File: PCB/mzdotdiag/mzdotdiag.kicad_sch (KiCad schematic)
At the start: 1 part, among them J1 Conn_01x25

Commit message: advancements in schematic
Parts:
- added Q1: Q_NPN_BEC, symbol Device:Q_NPN_BEC
- added U1: 4050, symbol 4xxx:4050
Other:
- note added: "B+ - 12V"
- note added: "F/P - Activate Fuel Pump Relay - Pull down to GND"
- note added: "FAB - Airbag SRS System - Feedback from SRS"
- note added: "FAT - Automatic Transmission - Feedback pin for AT"
- note added: "FBS - ABS System - Feedback from ABS"
- note added: "FEN - 0...12V - Low Active CEL Light"
- note added: "FSC - Cruise Control System - Cruise Control System Feedback Pin"
- note added: "IG- - Rev Counter (RPM = 30/delta[T])"
- note added: "MEN - ???"
- note added: "TAB - Airbag SRS System - Pull down to GND for starting test"
- note added: "TAT - Automatic Transmission - Pull down to GND to start test"
- note added: "TBS - ABS System - Pull down to GND for starting test"
- note added: "TEN - Test engine - Pull down the GND for starting test"
- note added: "TFA - Test Fan - Pull down to GND to start Fan"
- note added: "TSC - Cruise Control System - Test Cruise Control System"
- moved on the sheet: J1

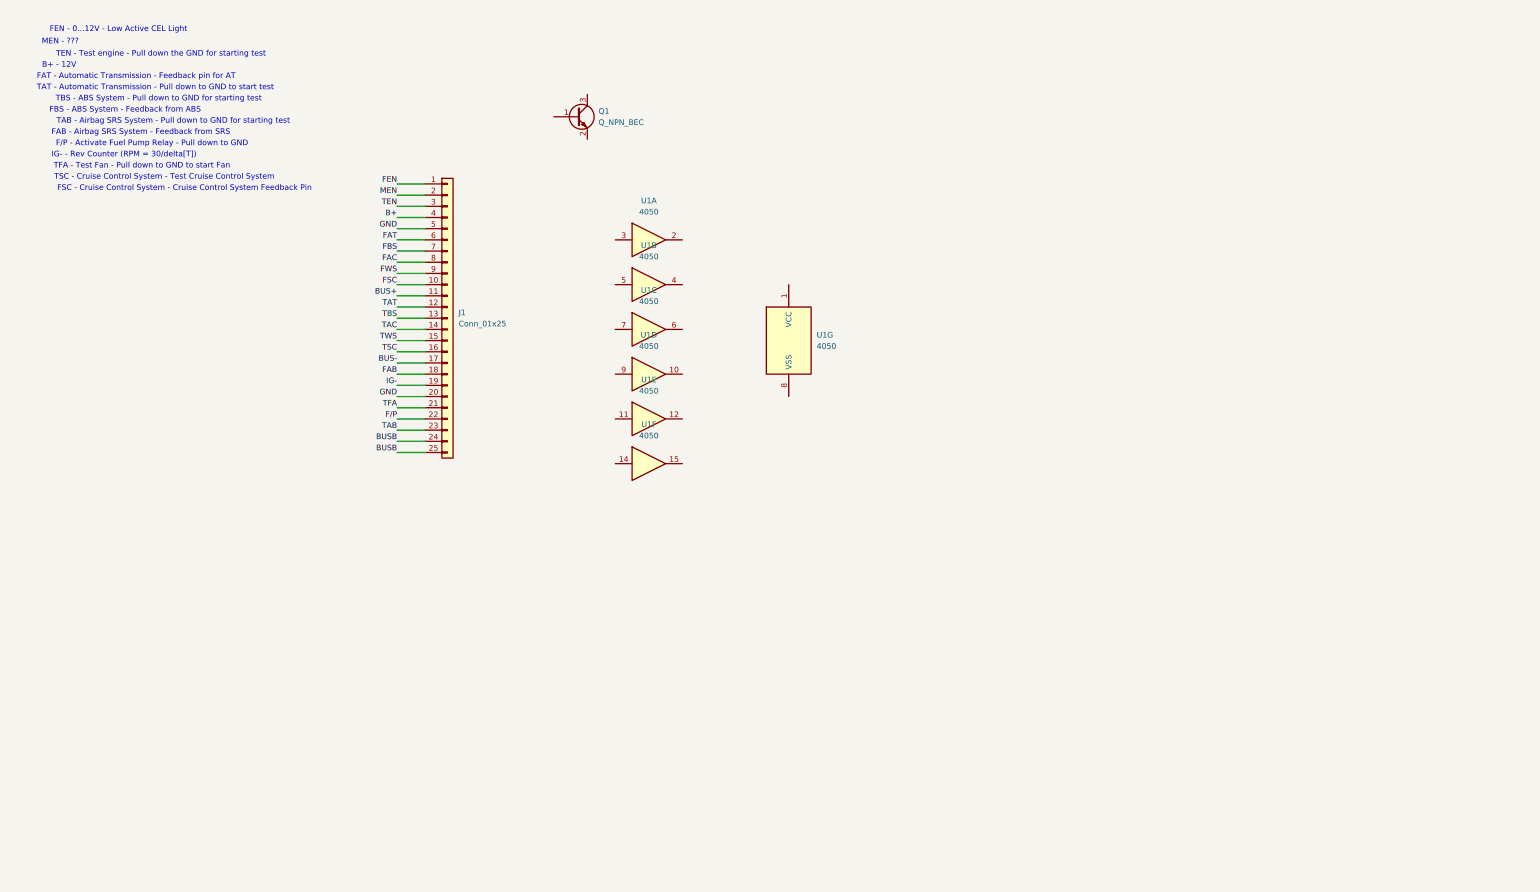
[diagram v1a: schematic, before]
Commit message: Schematic updates
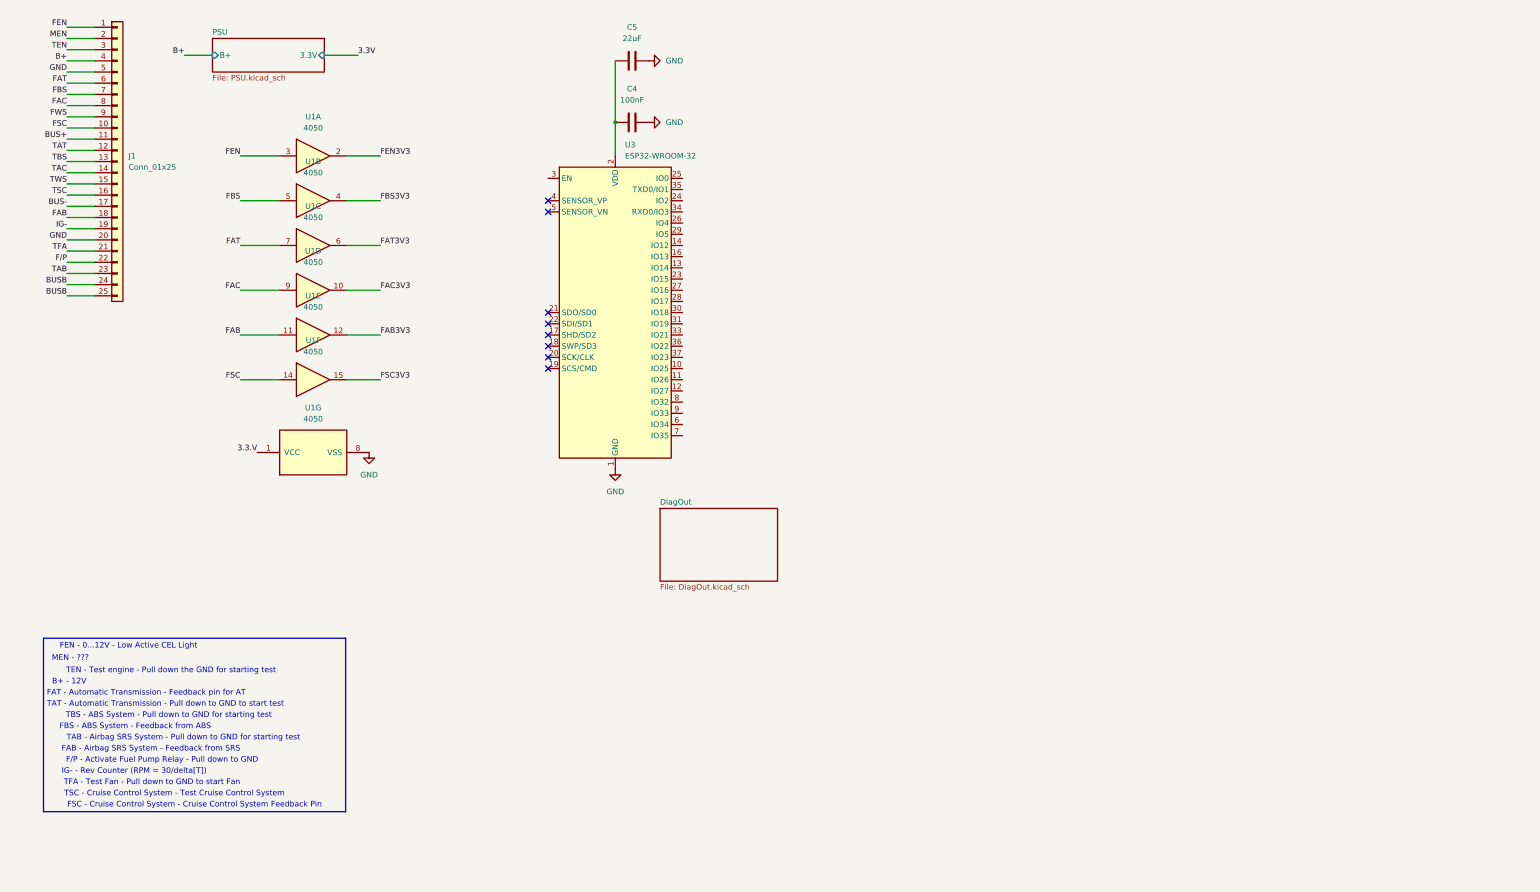
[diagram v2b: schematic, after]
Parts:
- removed Q1: Q_NPN_BEC, symbol Device:Q_NPN_BEC
- added C4: 100nF, symbol Device:C
- added C5: 22uF, symbol Device:C
- added U3: ESP32-WROOM-32, RF_Module:ESP32-WROOM-32, symbol RF_Module:ESP32-WROOM-32
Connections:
- net FAB: now also U1.11
- net FAC: now also U1.9
- net FAT: now also U1.7
- net FBS: now also U1.5
- net FEN: now also U1.3
- net FSC: now also U1.14
- net GND: now also U1.8 (VSS), C4.2, C5.2, U3.1 (GND), U3.15 (GND), U3.38 (GND), U3.39 (GND)
- net FBS3V3: now reaches U1.4
- net FSC3V3: now reaches U1.15
- net FAB3V3: now reaches U1.12
- net 3.3.V: now reaches U1.1 (VCC)
- net FAC3V3: now reaches U1.10
- net FAT3V3: now reaches U1.6
- net FEN3V3: now reaches U1.2
- new net: C4.1, C5.1, U3.2 (VDD)
- no-connect marks 0 -> 8
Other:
- added sheet DiagOut (DiagOut.kicad_sch)
- added sheet PSU (PSU.kicad_sch)
- moved on the sheet: J1, U1A, U1B, U1C, U1D, U1E, U1F, U1G

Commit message: Lots of schematic updates, found CD4504B for logic level shifting
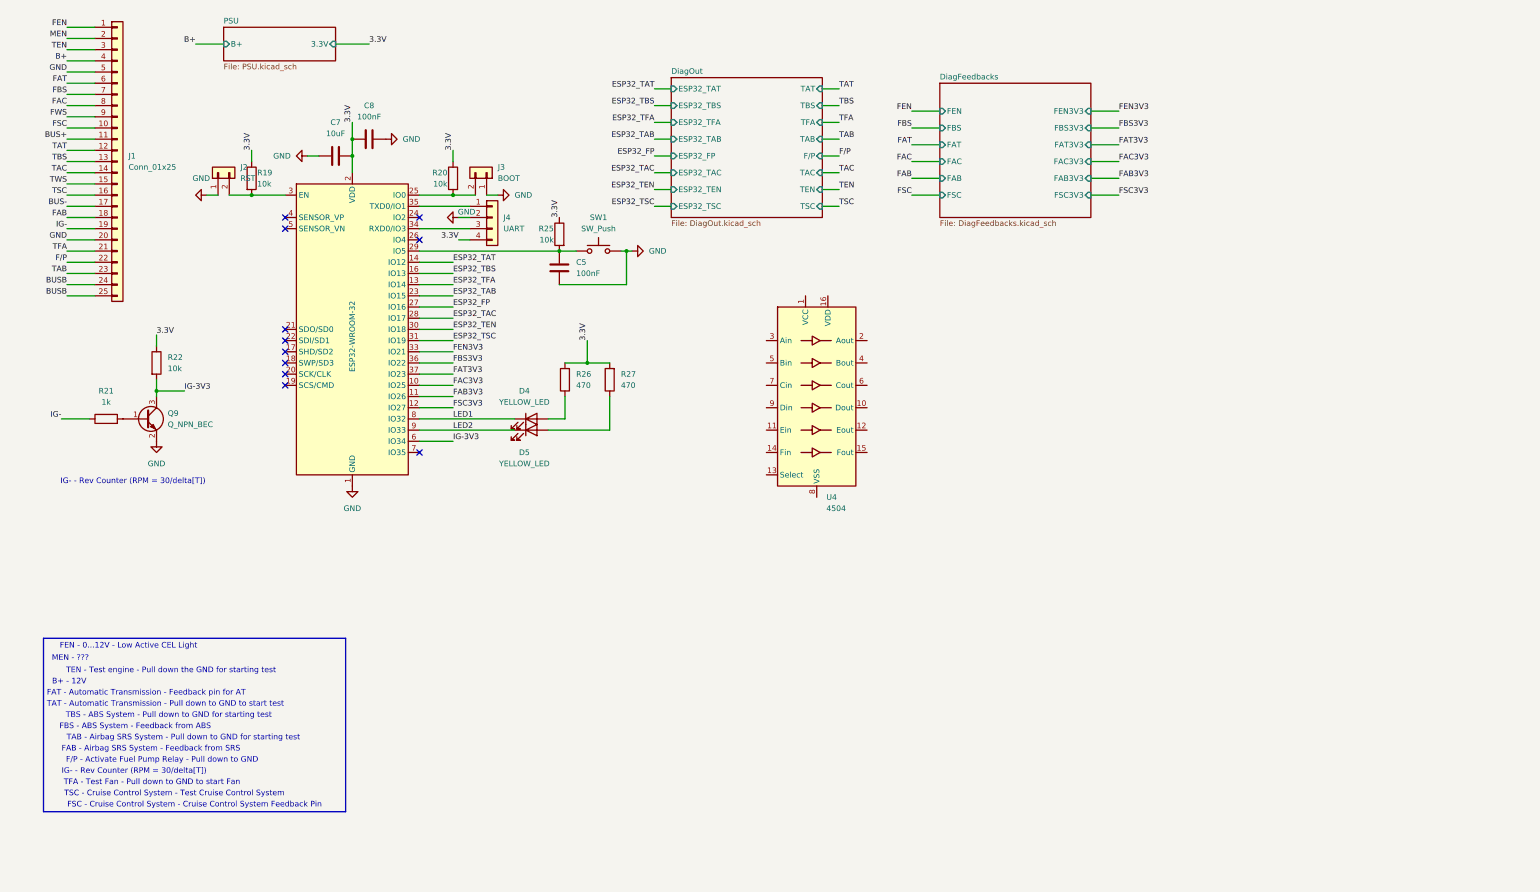
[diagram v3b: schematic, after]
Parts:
- removed C4: 100nF, symbol Device:C
- removed U1: 4050, symbol 4xxx:4050
- added C7: 10uF, Capacitor_SMD:C_0805_2012Metric, symbol Device:C
- added C8: 100nF, Capacitor_SMD:C_0603_1608Metric, symbol Device:C
- added D4, D5: YELLOW_LED, LED_SMD:LED_0805_2012Metric, symbol Device:LED
- added J2: RST, Button_Switch_SMD:SW_SPST_CK_RS282G05A3, symbol Connector_Generic:Conn_01x02
- added J3: BOOT, Button_Switch_SMD:SW_SPST_CK_RS282G05A3, symbol Connector_Generic:Conn_01x02
- added J4: UART, Connector_PinHeader_2.54mm:PinHeader_1x04_P2.54mm_Vertical, symbol Connector_Generic:Conn_01x04
- added Q9: Q_NPN_BEC, Package_TO_SOT_SMD:SOT-23, symbol Device:Q_NPN_BEC
- added R19, R20, R22, R25: 10k, Resistor_SMD:R_0603_1608Metric, symbol Device:R
- added R21: 1k, Resistor_SMD:R_0603_1608Metric, symbol Device:R
- added R26, R27: 470, Resistor_SMD:R_0603_1608Metric_Pad0.98x0.95mm_HandSolder, symbol Device:R
- added SW1: SW_Push, Button_Switch_SMD:SW_SPST_CK_RS282G05A3, symbol Switch:SW_Push
- added U4: 4504, symbol 4xxx:4504
- C5: value 22uF -> 100nF; footprint (none) -> Capacitor_SMD:C_0603_1608Metric; LOMEX (none) -> 82-13-28
- J1: footprint (none) -> mykicad_6:MazdaNADiag; Mouser (none) -> 651-1945193
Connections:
- net 3.3V: now also U3.2 (VDD), C7.1, C8.1, J4.4 (Pin_4), R19.1, R20.1, R22.1, R25.1, R26.2, R27.2
- net FAB3V3: now also U3.11 (IO26)
- net FAC3V3: now also U3.10 (IO25)
- net FAT3V3: now also U3.37 (IO23)
- net FBS3V3: now also U3.36 (IO22)
- net FEN3V3: now also U3.33 (IO21)
- net FSC3V3: now also U3.12 (IO27)
- net GND: now also C5.1, C7.2, C8.2, J2.1 (Pin_1), J3.1 (Pin_1), J4.2 (Pin_2), Q9.2 (E), SW1.2; no longer C5.2
- net IG-: now also R21.1
- net ESP32_TFA: now reaches U3.13 (IO14)
- net ESP32_TAT: now reaches U3.14 (IO12)
- net ESP32_TBS: now reaches U3.16 (IO13)
- net ESP32_TAB: now reaches U3.23 (IO15)
- net at U3.25 (IO0): now also J3.2 (Pin_2), R20.2
- net ESP32_FP: now reaches U3.27 (IO16)
- net ESP32_TAC: now reaches U3.28 (IO17)
- net at U3.29 (IO5): now also C5.2, R25.2, SW1.1
- net at U3.3 (EN): now also J2.2 (Pin_2), R19.2
- net ESP32_TEN: now reaches U3.30 (IO18)
- net ESP32_TSC: now reaches U3.31 (IO19)
- net at U3.34 (RXD0/IO3): now also J4.3 (Pin_3)
- net at U3.35 (TXD0/IO1): now also J4.1 (Pin_1)
- net IG-3V3: now reaches U3.6 (IO34)
- net IG-3V3: now also Q9.3 (C), R22.2
- net LED1: now reaches U3.8 (IO32)
- net LED1: now also D4.1 (K)
- net LED2: now reaches U3.9 (IO33)
- net LED2: now also D5.1 (K)
- new net: Q9.1 (B), R21.2
- new net: D4.2 (A), R26.1
- new net: D5.2 (A), R27.1
- no-connect marks 8 -> 11
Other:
- added sheet DiagFeedbacks (DiagFeedbacks.kicad_sch)
- sheet DiagOut ports: added ESP32_FP, ESP32_TAB, ESP32_TAC, ESP32_TAT, ESP32_TBS, ESP32_TEN, ESP32_TFA, ESP32_TSC, F/P, TAB, TAC, TAT, TBS, TEN, TFA, TSC; removed none

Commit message: schematic and pcb update with new levelshifter IC
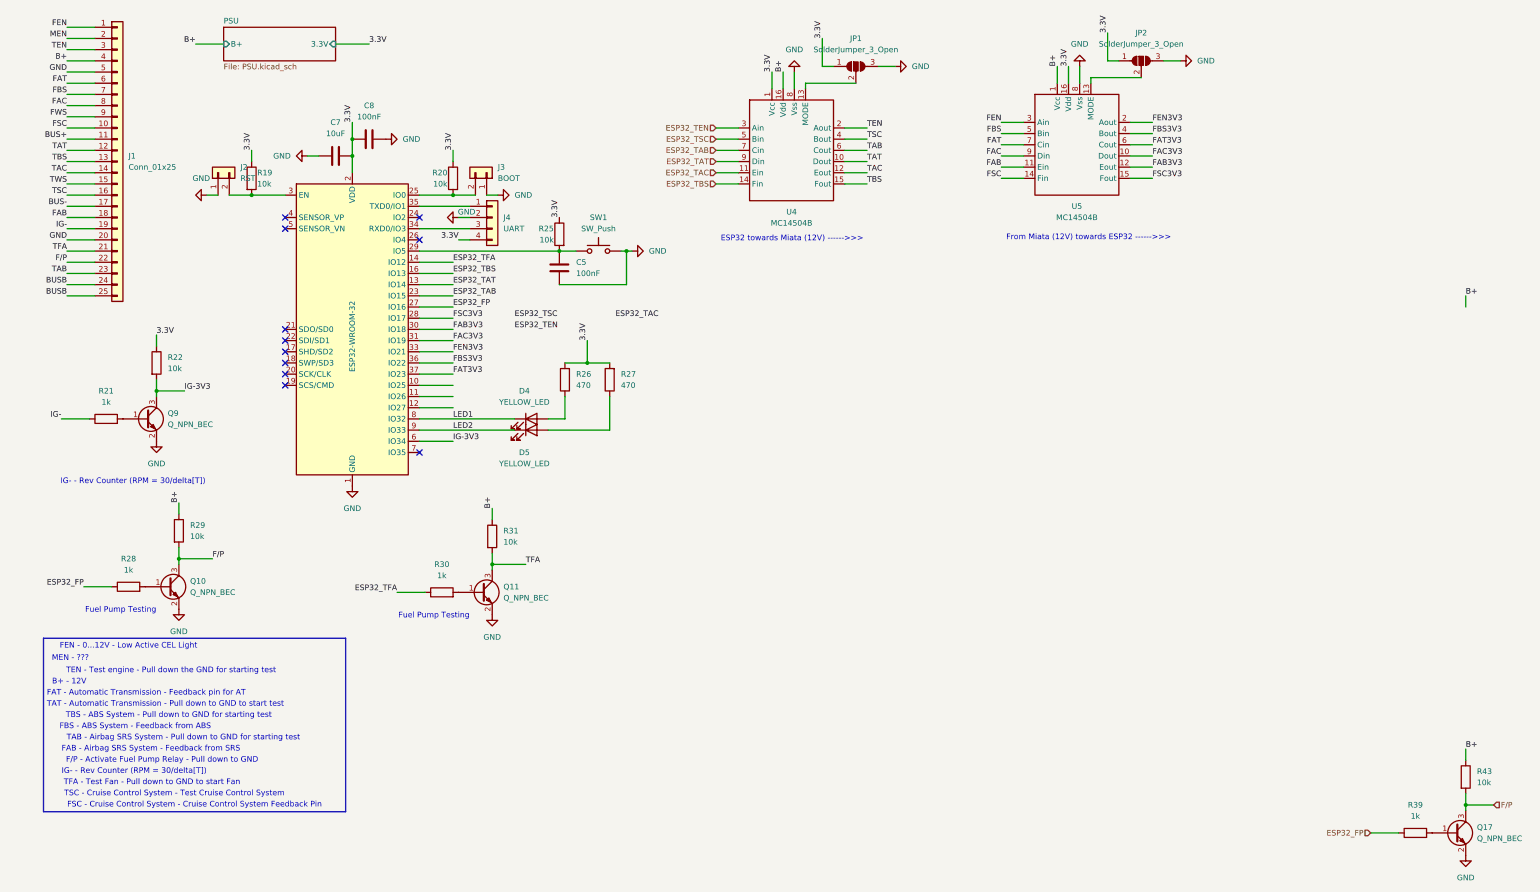
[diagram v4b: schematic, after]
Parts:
- removed U4: 4504, symbol 4xxx:4504
- added JP1, JP2: SolderJumper_3_Open, Jumper:SolderJumper-3_P1.3mm_Open_RoundedPad1.0x1.5mm, symbol Jumper:SolderJumper_3_Open
- added Q10, Q11, Q17: Q_NPN_BEC, Package_TO_SOT_SMD:SOT-23, symbol Device:Q_NPN_BEC
- added R28, R30, R39: 1k, Resistor_SMD:R_0603_1608Metric, symbol Device:R
- added R29, R31, R43: 10k, Resistor_SMD:R_0603_1608Metric, symbol Device:R
- added U4, U5: MC14504B, Package_SO:SOIC-16_3.9x9.9mm_P1.27mm, symbol local_lib:MC14504
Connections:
- net 3.3V: now also JP1.1 (A), JP2.1 (A), U4.1 (Vcc), U5.16 (Vdd)
- net B+: now also R29.1, R31.1, R43.1, U4.16 (Vdd), U5.1 (Vcc)
- net ESP32_FP: now also R28.1, R39.1
- net ESP32_TAB: now also U4.7 (Cin)
- net ESP32_TAC: now also U4.11 (Ein); no longer U3.28 (IO17)
- net ESP32_TAT: now also U3.13 (IO14), U4.9 (Din); no longer U3.14 (IO12)
- net ESP32_TBS: now also U4.14 (Fin)
- net ESP32_TEN: now also U4.3 (Ain); no longer U3.30 (IO18)
- net ESP32_TFA: now also U3.14 (IO12), R30.1; no longer U3.13 (IO14)
- net ESP32_TSC: now also U4.5 (Bin); no longer U3.31 (IO19)
- net FAB: now also U5.11 (Ein)
- net FAB3V3: now also U3.30 (IO18), U5.12 (Eout); no longer U3.11 (IO26)
- net FAC: now also U5.9 (Din)
- net FAC3V3: now also U3.31 (IO19), U5.10 (Dout); no longer U3.10 (IO25)
- net FAT: now also U5.7 (Cin)
- net FAT3V3: now also U5.6 (Cout)
- net FBS: now also U5.5 (Bin)
- net FBS3V3: now also U5.4 (Bout)
- net FEN: now also U5.3 (Ain)
- net FEN3V3: now also U5.2 (Aout)
- net FSC: now also U5.14 (Fin)
- net FSC3V3: now also U3.28 (IO17), U5.15 (Fout); no longer U3.12 (IO27)
- net F/P: now also Q10.3 (C), Q17.3 (C), R29.2, R43.2
- net GND: now also JP1.3 (B), JP2.3 (B), Q10.2 (E), Q11.2 (E), Q17.2 (E), U4.8 (Vss), U5.8 (Vss)
- net TAB: now also U4.6 (Cout)
- net TAC: now also U4.12 (Eout)
- net TAT: now also U4.10 (Dout)
- net TBS: now also U4.15 (Fout)
- net TEN: now also U4.2 (Aout)
- net TFA: now also Q11.3 (C), R31.2
- net TSC: now also U4.4 (Bout)
- new net: Q10.1 (B), R28.2
- new net: JP1.2 (C), U4.13 (MODE)
- new net: JP2.2 (C), U5.13 (MODE)
- new net: Q11.1 (B), R30.2
- new net: Q17.1 (B), R39.2
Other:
- removed sheet DiagFeedbacks
- removed sheet DiagOut
- note added: "ESP32 towards Miata (12V) ------>>>"
- note added: "From Miata (12V) towards ESP32 ------>>>"
- note added: "Fuel Pump Testing"

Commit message: pcb upd
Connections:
- net ESP32_TAB: now also U3.14 (IO12); no longer U3.23 (IO15)
- net ESP32_TBS: no longer U3.16 (IO13)
- net ESP32_TEN: now also U3.23 (IO15)
- net ESP32_TFA: no longer U3.14 (IO12)
- net ESP32_TSC: now also U3.16 (IO13)
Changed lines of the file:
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@@
-		)
-	)
-	(label "ESP32_TBS"
-		(at 107.95 72.39 0)
-		(effects
-			(font
-				(size 1.27 1.27)
-			)
-			(justify left bottom)
 		)
 	)
@@
 		)
 	)
+	(label "ESP32_TFA"
+		(at 138.43 81.28 0)
+		(effects
+			(font
+				(size 1.27 1.27)
+			)
+			(justify left bottom)
+		)
+	)
 	(label "FEN3V3"
 		(at 266.7 38.1 0)
@@
 		)
 	)
-	(label "ESP32_TAB"
-		(at 107.95 77.47 0)
-		(effects
-			(font
-				(size 1.27 1.27)
-			)
-			(justify left bottom)
-		)
-	)
 	(label "FAT"
 		(at 20.32 29.21 180)
@@
 		)
 	)
+	(label "ESP32_TAB"
+		(at 107.95 69.85 0)
+		(effects
+			(font
+				(size 1.27 1.27)
+			)
+			(justify left bottom)
+		)
+	)
 	(label "TAB"
 		(at 201.93 44.45 0)
@@
 		)
 	)
+	(label "ESP32_TBS"
+		(at 121.92 80.01 0)
+		(effects
+			(font
+				(size 1.27 1.27)
+			)
+			(justify left bottom)
+		)
+	)
 	(label "3.3V"
 		(at 247.65 25.4 90)
@@
 	)
 	(label "ESP32_TEN"
-		(at 121.92 85.09 0)
+		(at 107.95 77.47 0)
 		(effects
 			(font
@@
 	)
 	(label "ESP32_TSC"
-		(at 121.92 82.55 0)
+		(at 107.95 72.39 0)
 		(effects
 			(font
@@
 		)
 	)
-	(label "ESP32_TFA"
-		(at 107.95 69.85 0)
-		(effects
-			(font
-				(size 1.27 1.27)
-			)
-			(justify left bottom)
-		)
-	)
 	(label "3.3V"
 		(at 132.08 59.69 90)
@@
 	)
 	(label "ESP32_TAC"
-		(at 144.78 82.55 0)
-		(effects
-			(font
+		(at 121.92 87.63 0)
+		(effects
+			(font

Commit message: finished wiring
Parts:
- removed Q17: Q_NPN_BEC, Package_TO_SOT_SMD:SOT-23, symbol Device:Q_NPN_BEC
- removed R39: 1k, Resistor_SMD:R_0603_1608Metric, symbol Device:R
- removed R43: 10k, Resistor_SMD:R_0603_1608Metric, symbol Device:R
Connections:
- net B+: no longer R29.1, R31.1, U4.16 (Vdd), U5.1 (Vcc)
- net ESP32_TAC: now also U3.12 (IO27)
- net ESP32_TBS: now also U3.11 (IO26)
- net ESP32_TFA: now also U3.10 (IO25)
- new net B+_PROT: R29.1, R31.1, U4.16 (Vdd), U5.1 (Vcc)
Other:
- sheet PSU ports: added B+_PROT; removed none

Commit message: order files and pcb done
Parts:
- U3: Mouser (none) -> 356-ESP32WRM32E128PH
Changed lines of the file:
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@@
 			)
 		)
-		(property "Mouser" ""
+		(property "Mouser" "356-ESP32WRM32E128PH "
 			(at 85.09 85.09 0)
 			(effects
